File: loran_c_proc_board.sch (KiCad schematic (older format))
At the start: 32 parts, among them P101 Power, P102 Cortex SWD, P103 Clock board, U101 LD1117S33, U102 74AC14, U103 74AC14

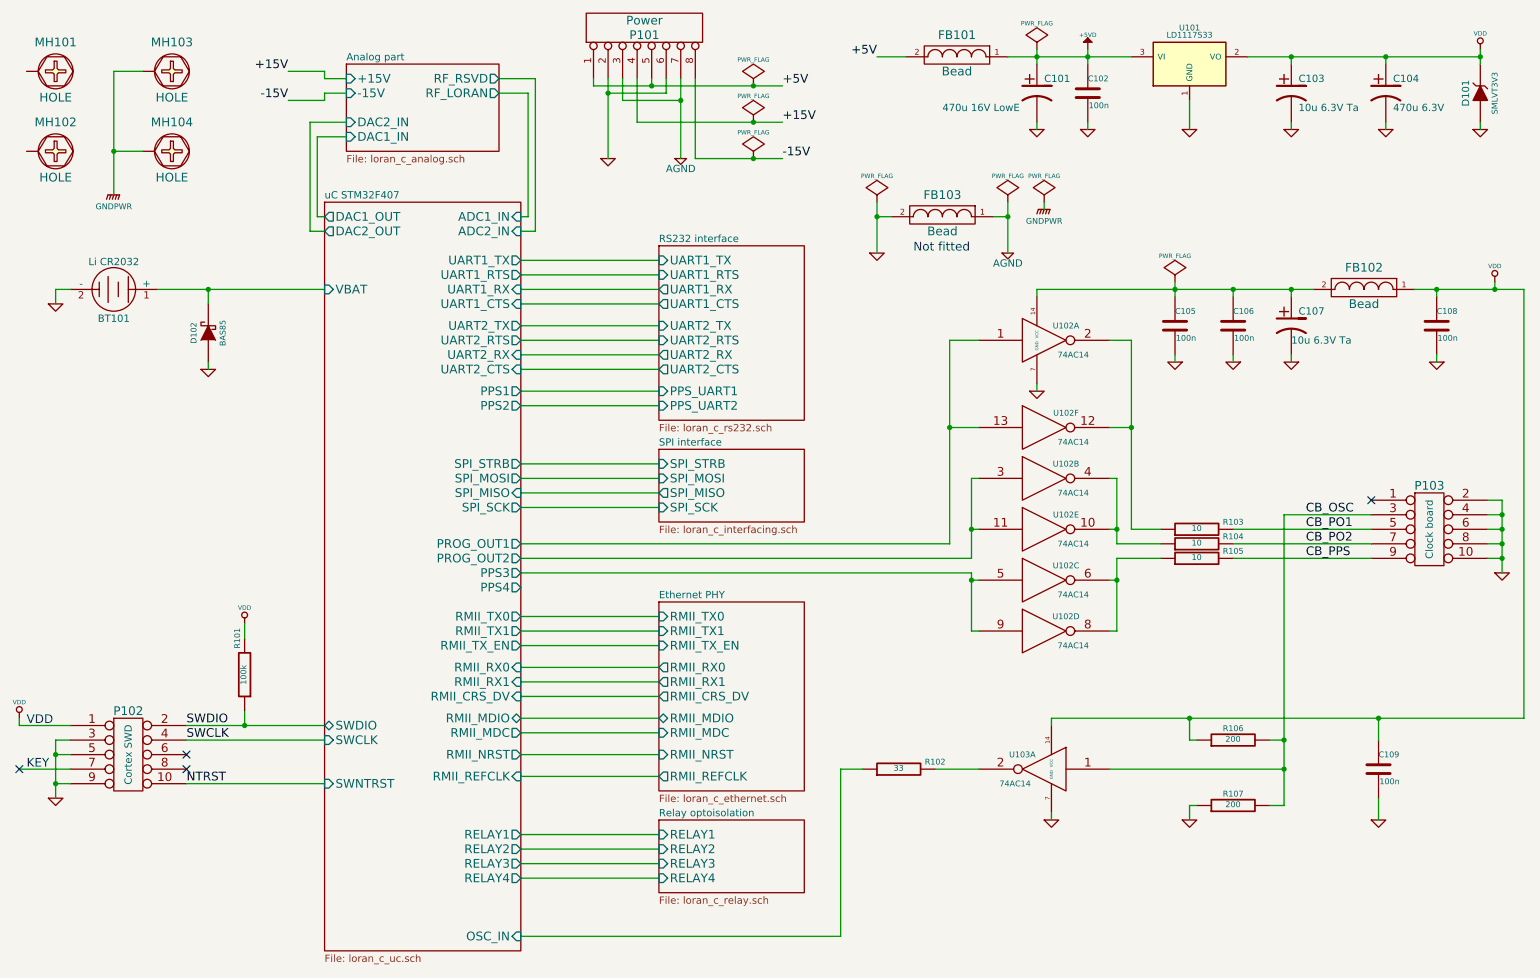
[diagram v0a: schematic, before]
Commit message: Update: lots of refactoring and pin remap ..In chase for easier PCB routing PCB still not completed
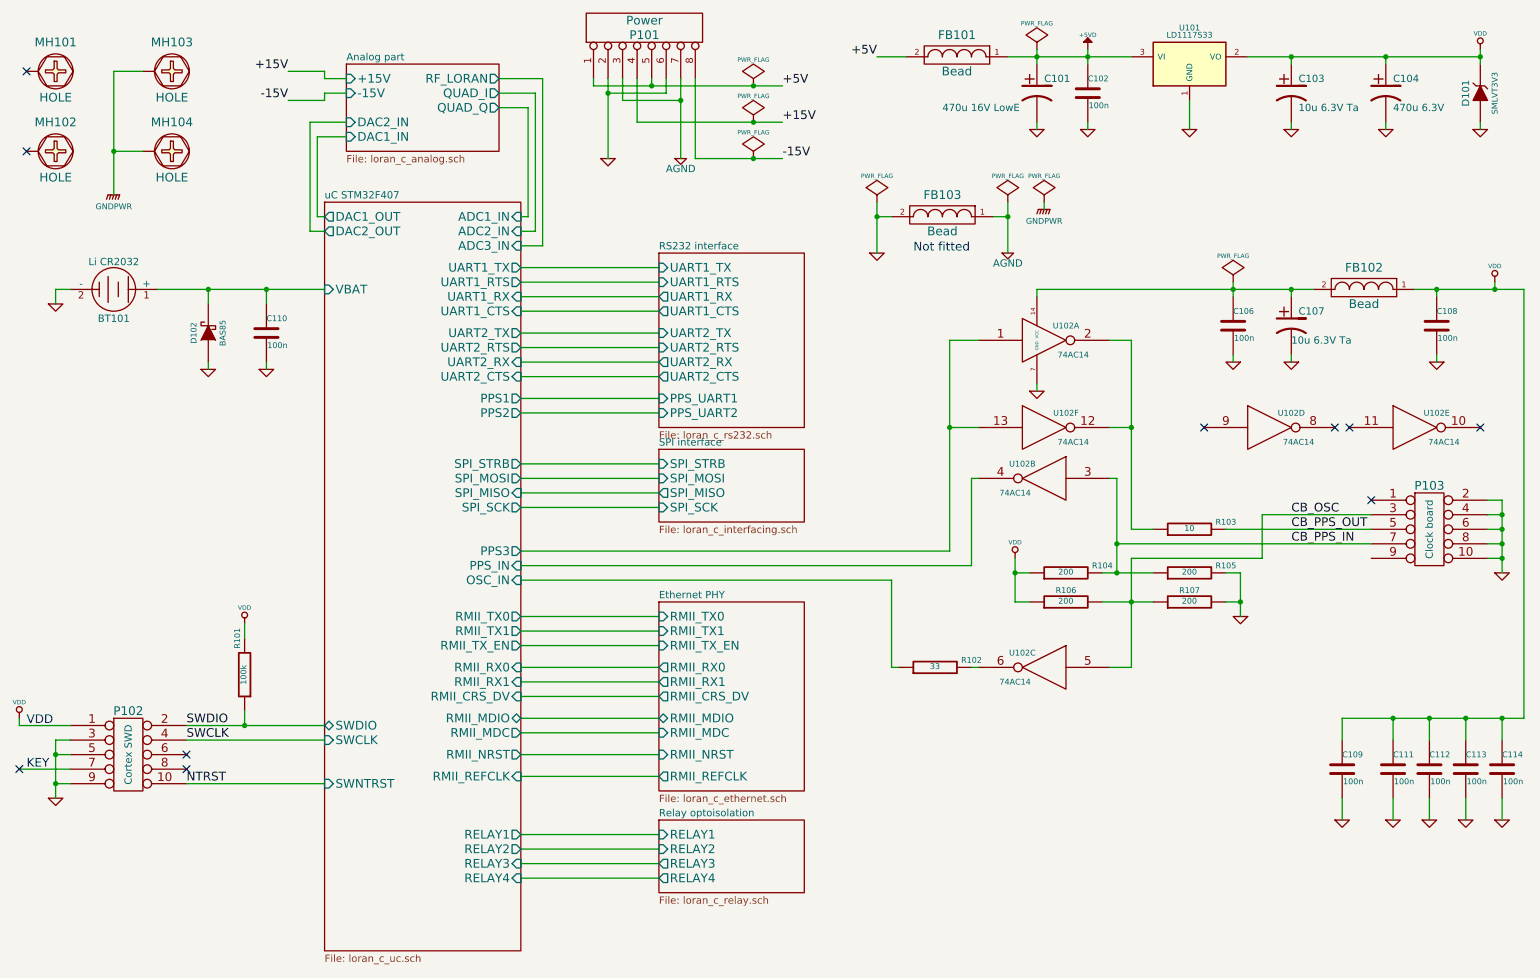
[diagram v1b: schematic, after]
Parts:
- removed C105: 100n, w_smd_capacitors:c_1206, symbol C
- removed U103: 74AC14, w_smd_dil:so-16, symbol 74HC14
- added C110: 100n, w_smd_capacitors:c_0805, symbol C
- added C111, C112, C113, C114: 100n, w_smd_capacitors:c_1206, symbol C
- R104, R105: value 10 -> 200
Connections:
- net uC STM32F407/PROG_OUT1 is gone; now on net uC STM32F407/PPS3: U102.1, U102.13
- net CB_OSC: now also R107.1, U102.5; no longer R107.2
- net GND: now also R105.2, R107.2, C110.2, C111.2, C112.2, C113.2, C114.2; no longer R107.1
- net VDD: now also R104.1, C111.1, C112.1, C113.1, C114.1
- net uC STM32F407/PPS3: no longer U102.5, U102.9
- net uC STM32F407/VBAT: now also C110.1
- net at R102.2: now also U102.6
- net CB_PO1 renamed CB_PPS_OUT
- net CB_PO2 renamed CB_PPS_IN
- net CB_PPS_IN: now also R105.1, U102.3
- net CB_PPS: no longer names the net of P103.9
- net CB_PPS: no longer R105.2
- net uC STM32F407/PROG_OUT2: no longer names the net of U102.11
- net uC STM32F407/PROG_OUT2: no longer U102.3
- new net uC STM32F407/PPS_IN: U102.4
- now unconnected: U102.10, U102.8
- no-connect marks 4 -> 10
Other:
- moved on the sheet: C109, R102, R103, R104, R105, R106, R107, U102C, U102D, U102E

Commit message: Update: PCB routing still in process...
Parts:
- removed C112, C113, C114: 100n, w_smd_capacitors:c_1206, symbol C
- added R108: 33, w_smd_resistors:r_1206, symbol R
- renumbered C111 to C110, C110 to C111
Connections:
- net CB_OSC: now also R104.1, R105.2, U102.13; no longer R106.2, R107.1, U102.5
- net CB_PPS_IN: now also R106.1, R107.2, U102.9; no longer R104.2, R105.1, U102.3
- net GND: now also R105.1, R107.1, U102.5; no longer R105.2, R107.2
- net VDD: now also FB102.2; no longer C109.1, C110.1, FB102.1, R104.1, R106.1
- net uC STM32F407/PPS3: now also U102.11, U102.3; no longer U102.1, U102.13
- net uC STM32F407/PPS_IN: now also R108.1; no longer U102.4
- net CBL_VDD: now reaches C106.1, C107.1, U102.14 (VCC)
- net CBL_VDD: now also C109.1, C110.1, FB102.1, R104.2, R106.2, U102.1; no longer FB102.2
- net at U102.10: now also R103.1, U102.4
- net at R102.2: now also U102.12; no longer U102.6
- net at U102.8: now also R108.2
- now unconnected: U102.2
- no-connect marks 10 -> 8
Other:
- moved on the sheet: C109, C110, R104, R105, R106, R107, U102B, U102C, U102D, U102E, U102F

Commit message: Update: PCB almost finished (3D views also up-to-date)
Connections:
- net CBL_VDD: no longer U102.1
- net GND: now also U102.1
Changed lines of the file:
@@
 LIBS:led_holder
 LIBS:crystal_shielded
+LIBS:conn_2s
 LIBS:loran_c_proc_board-cache
 EELAYER 24 0
@@
 	7750 2750 7750 2800
 Wire Wire Line
-	7300 2750 9650 2750
-Wire Wire Line
 	9500 2700 9500 2800
 Wire Wire Line
@@
 CBL_VDD
 Wire Wire Line
-	7350 3100 7300 3100
-Wire Wire Line
-	7300 3100 7300 2750
-Connection ~ 7750 2750
+	7250 3100 7350 3100
 Wire Wire Line
 	9900 3700 9800 3700
@@
 Wire Wire Line
 	9100 5950 9100 6100
+Wire Wire Line
+	7750 2750 9650 2750
+Wire Wire Line
+	7250 3100 7250 3450
+$Comp
+L GND #PWR040
+U 1 1 53089649
+P 7250 3450
+F 0 "#PWR040" H 7250 3450 30  0001 C CNN
+F 1 "GND" H 7250 3380 30  0001 C CNN
+F 2 "" H 7250 3450 60  0000 C CNN
+F 3 "" H 7250 3450 60  0000 C CNN
+	1    7250 3450
+	1    0    0    -1
+$EndComp
 $EndSCHEMATC
